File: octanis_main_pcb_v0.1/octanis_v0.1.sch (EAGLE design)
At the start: 83 parts, among them IC1 REG1117, Q1 32.768kHz, T1 BC547, T2 BC547, U1 BQ24210, U2 BQ27510_DRZ_12, U3 DRV8836DSSR, U4 DRV8836DSSR, U5 DRV8836DSSR, U6 MSP430F5529IPNR, U7 DRV8836DSSR, U9 BMP180

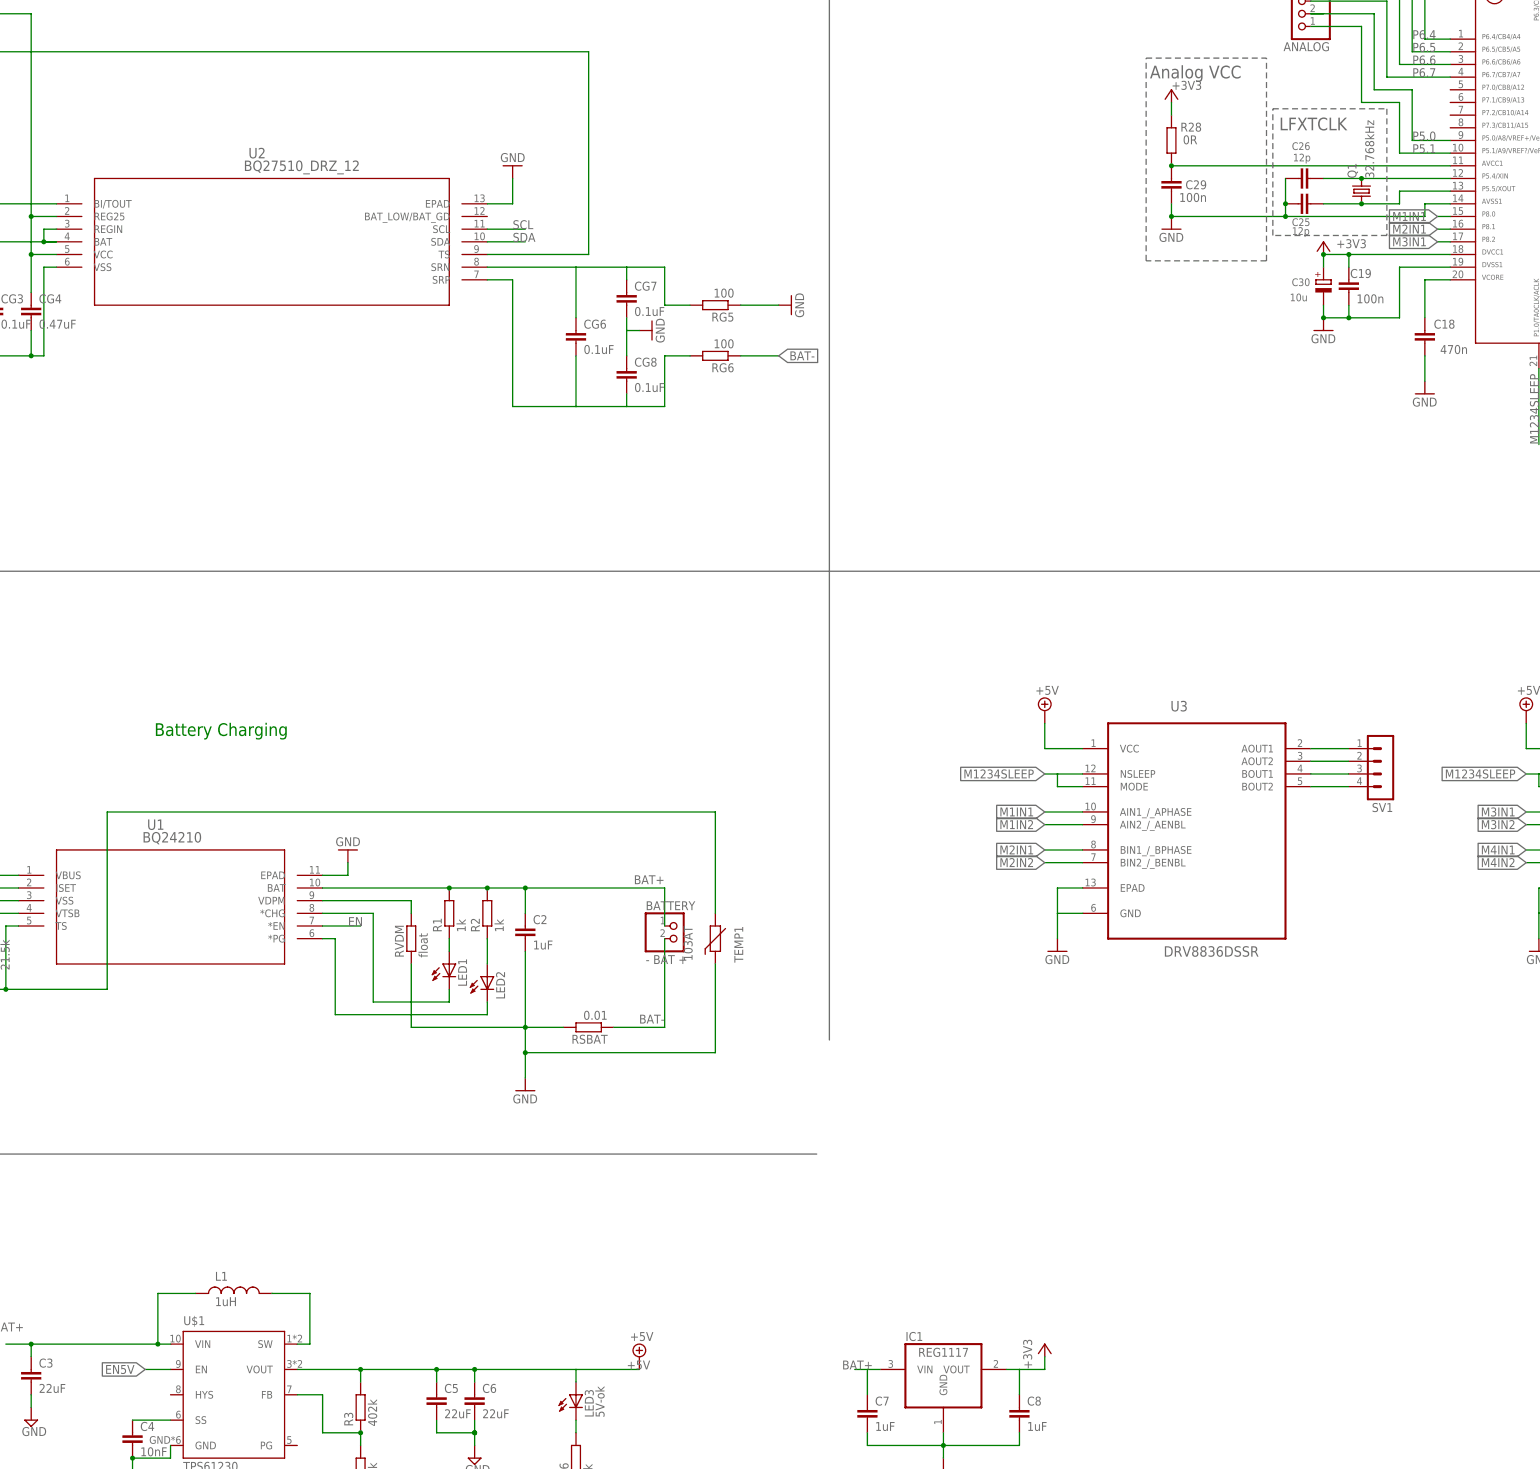
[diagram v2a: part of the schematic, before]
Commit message: increased space between traces, connected ch_en and 5Ven to uC
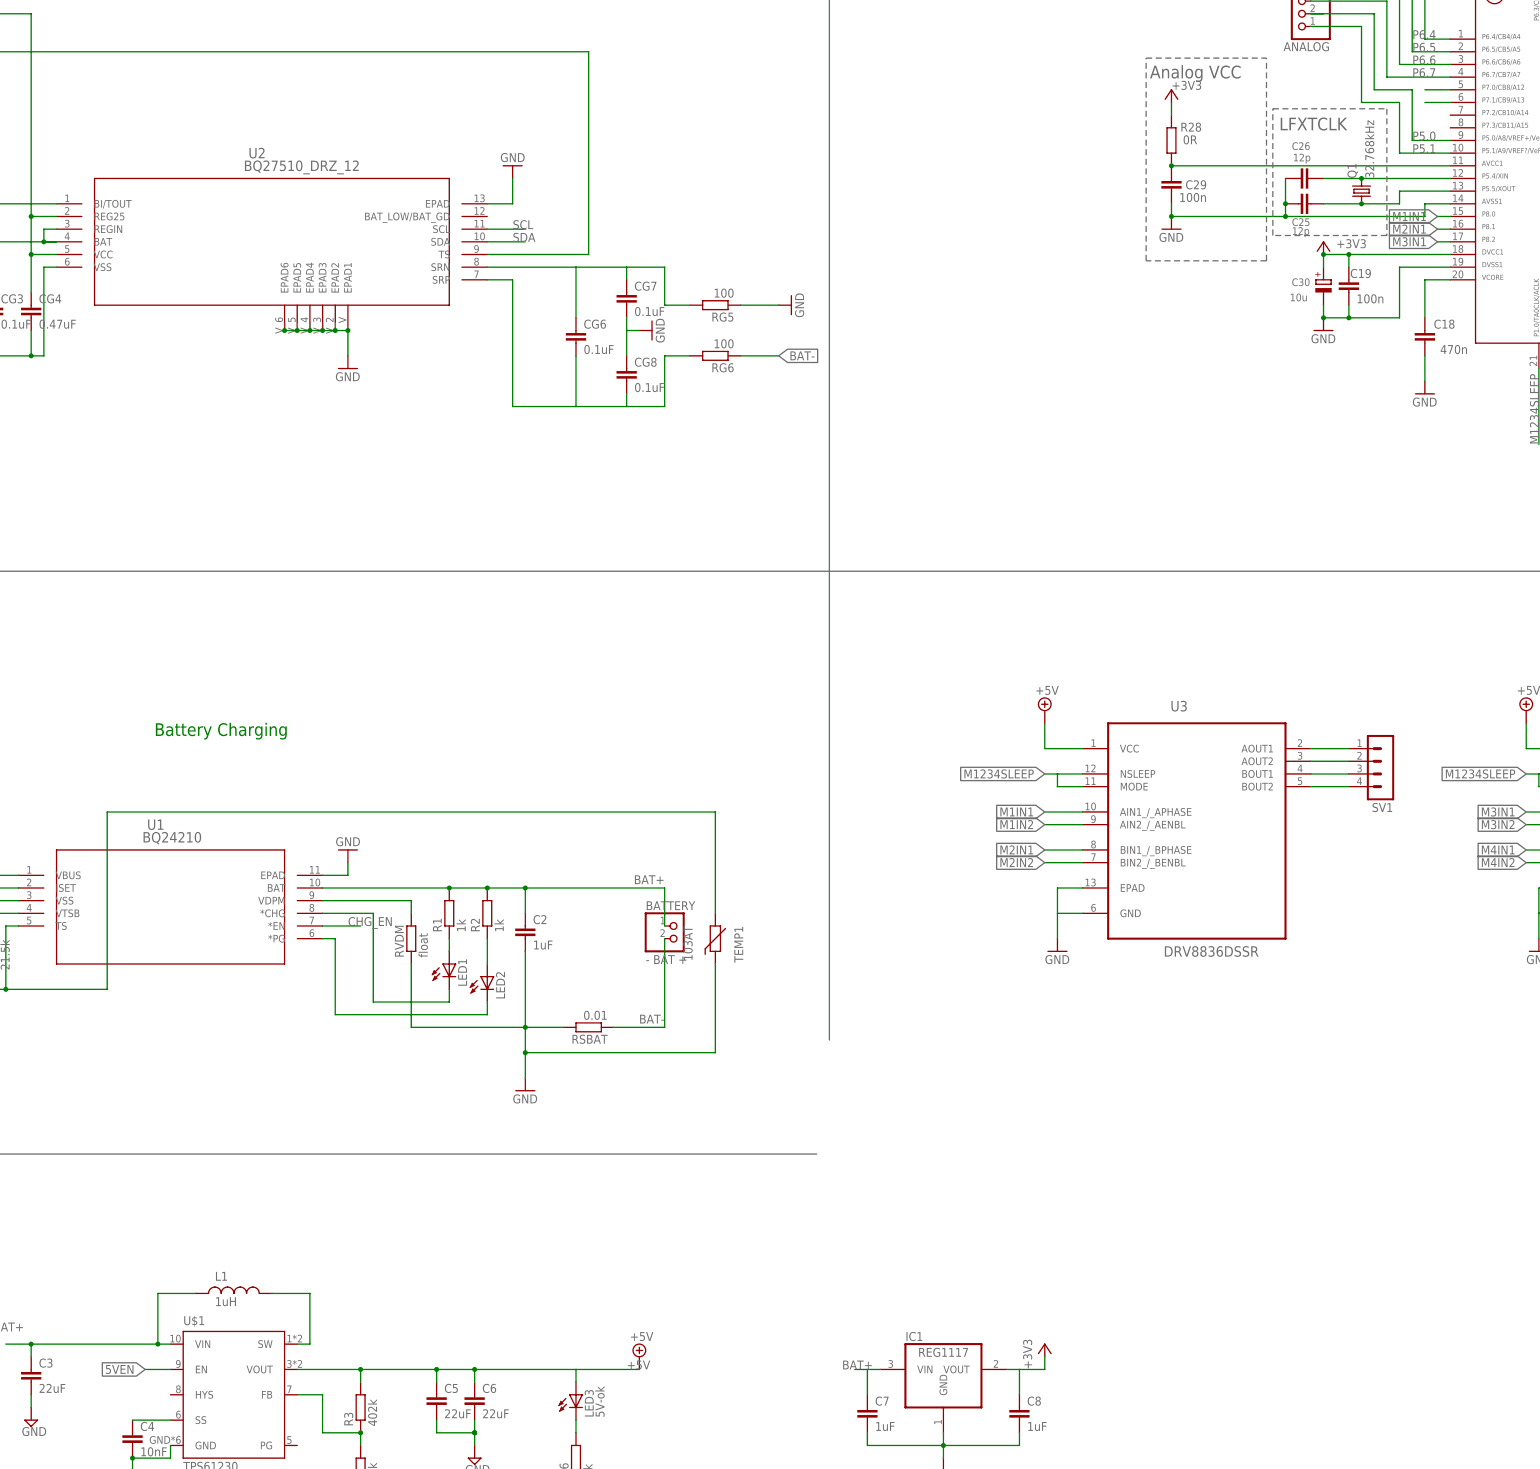
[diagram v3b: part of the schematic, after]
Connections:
- removed net EN: U1.*EN
- removed net EN5V: U$1.EN
- new net 5VEN: U$1.EN, U6.6
- new net CHG_EN: U1.*EN, U6.5
- net GND: now also U2.EPAD1, U2.EPAD2, U2.EPAD3, U2.EPAD4, U2.EPAD5, U2.EPAD6
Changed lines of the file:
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@@
 <part name="DIGITAL1" library="pinhead" deviceset="PINHD-1X6" device="" value="DIGITAL1"/>
 <part name="DIGITAL2" library="pinhead" deviceset="PINHD-1X8" device="" value="DIGITAL2"/>
+<part name="GND31" library="supply1" deviceset="GND" device=""/>
 </parts>
 <sheets>
@@
 <instance part="DIGITAL1" gate="A" x="391.16" y="157.48" rot="R270"/>
 <instance part="DIGITAL2" gate="A" x="416.56" y="241.3"/>
+<instance part="GND31" gate="1" x="91.44" y="185.42"/>
 </instances>
 <busses>
@@
 <pinref part="GND32" gate="1" pin="GND"/>
 </segment>
+<segment>
+<pinref part="U2" gate="A" pin="EPAD6"/>
+<pinref part="U2" gate="A" pin="EPAD1"/>
+<wire x1="78.74" y1="193.04" x2="81.28" y2="193.04" width="0.1524" layer="91"/>
+<wire x1="81.28" y1="193.04" x2="83.82" y2="193.04" width="0.1524" layer="91"/>
+<wire x1="83.82" y1="193.04" x2="86.36" y2="193.04" width="0.1524" layer="91"/>
+<wire x1="86.36" y1="193.04" x2="88.9" y2="193.04" width="0.1524" layer="91"/>
+<wire x1="88.9" y1="193.04" x2="91.44" y2="193.04" width="0.1524" layer="91"/>
+<wire x1="91.44" y1="193.04" x2="91.44" y2="187.96" width="0.1524" layer="91"/>
+<pinref part="GND31" gate="1" pin="GND"/>
+<junction x="78.74" y="193.04"/>
+<pinref part="U2" gate="A" pin="EPAD5"/>
+<junction x="81.28" y="193.04"/>
+<pinref part="U2" gate="A" pin="EPAD4"/>
+<junction x="83.82" y="193.04"/>
+<pinref part="U2" gate="A" pin="EPAD3"/>
+<junction x="86.36" y="193.04"/>
+<pinref part="U2" gate="A" pin="EPAD2"/>
+<junction x="88.9" y="193.04"/>
+<junction x="91.44" y="193.04"/>
+</segment>
 </net>
 <net name="BAT+" class="3">
@@
 </segment>
 </net>
-<net name="EN" class="0">
+<net name="CHG_EN" class="0">
 <segment>
 <pinref part="U1" gate="A" pin="*EN"/>
 <wire x1="86.36" y1="73.66" x2="93.98" y2="73.66" width="0.1524" layer="91"/>
 <label x="91.44" y="73.66" size="1.778" layer="95"/>
+</segment>
+<segment>
+<pinref part="U6" gate="G$1" pin="5"/>
+<wire x1="312.42" y1="241.3" x2="307.34" y2="241.3" width="0.1524" layer="91"/>
 </segment>
 </net>
@@
 </segment>
 </net>
-<net name="EN5V" class="0">
+<net name="5VEN" class="0">
 <segment>
 <pinref part="U$1" gate="G$1" pin="EN"/>
@@
 <label x="50.8" y="-15.24" size="1.778" layer="95" rot="R180" xref="yes"/>
 </segment>
-</net>
+<segment>
+<pinref part="U6" gate="G$1" pin="6"/>
+<wire x1="312.42" y1="238.76" x2="307.34" y2="238.76" width="0.1524" layer="91"/>
+</segment>
+</net>

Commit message: most recent version
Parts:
- R3: value 402k -> 270k
- R5: value 100k -> 68k
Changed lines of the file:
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@@
 <part name="C4" library="rcl" deviceset="C-EU" device="C0603" value="10nF"/>
 <part name="SUPPLY2" library="supply2" deviceset="GND" device=""/>
-<part name="R3" library="rcl" deviceset="R-EU_" device="R0603" value="402k"/>
-<part name="R5" library="rcl" deviceset="R-EU_" device="R0603" value="100k"/>
+<part name="R3" library="rcl" deviceset="R-EU_" device="R0603" value="270k"/>
+<part name="R5" library="rcl" deviceset="R-EU_" device="R0603" value="68k"/>
 <part name="SUPPLY3" library="supply2" deviceset="GND" device=""/>
 <part name="C5" library="rcl" deviceset="C-EU" device="C0603" value="22uF"/>
